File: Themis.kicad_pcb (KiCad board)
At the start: 2 copper layers, 100 x 50 mm, 585 parts, among them J1 SMA, J10 Conn_01x01, J11 Conn_01x01, J12 Conn_01x01, J13 Conn_01x01, J14 SMA, J15 SMA, J16 SMA, J17 SMA, J18 Conn_01x01, J2 SMA, J20 Conn_01x01, J3 SMA, J4 SMA, J5 Conn_01x05, J6 SMA, J7 SMA, J8 SMA, J9 SMA, T1 Tr 1/33, T2 Tr 33/1, U1 LMC6482

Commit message: new stitching, new gerber
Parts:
- removed the REF** at (101.5, 126.0)
- removed the REF** at (100.5, 126.0)
- removed the REF** at (99.5, 126.0)
- removed the REF** at (98.5, 126.0)
- removed the REF** at (97.5, 126.0)
- removed the REF** at (96.5, 126.0)
- removed the REF** at (95.5, 126.0)
- removed the REF** at (101.5, 125.0)
- removed the REF** at (100.5, 125.0)
- removed the REF** at (99.5, 125.0)
- removed the REF** at (98.5, 125.0)
- removed the REF** at (97.5, 125.0)
- removed the REF** at (96.5, 125.0)
- removed the REF** at (95.5, 125.0)
- removed the REF** at (101.5, 124.0)
- removed the REF** at (100.5, 124.0)
- removed the REF** at (99.5, 124.0)
- removed the REF** at (98.5, 124.0)
- removed the REF** at (97.5, 124.0)
- removed the REF** at (96.5, 124.0)
- removed the REF** at (95.5, 124.0)
- removed the REF** at (101.5, 123.0)
- removed the REF** at (100.5, 123.0)
- removed the REF** at (99.5, 123.0)
- removed the REF** at (98.5, 123.0)
- removed the REF** at (97.5, 123.0)
- removed the REF** at (96.5, 123.0)
- removed the REF** at (95.5, 123.0)
- removed the REF** at (101.5, 122.0)
- removed the REF** at (100.5, 122.0)
- removed the REF** at (99.5, 122.0)
- removed the REF** at (98.5, 122.0)
- removed the REF** at (97.5, 122.0)
- removed the REF** at (96.5, 122.0)
- removed the REF** at (95.5, 122.0)
- removed the REF** at (101.5, 121.0)
- removed the REF** at (100.5, 121.0)
- removed the REF** at (99.5, 121.0)
- removed the REF** at (98.5, 121.0)
- removed the REF** at (97.5, 121.0)
- removed the REF** at (96.5, 121.0)
- removed the REF** at (95.5, 121.0)
- removed the REF** at (101.5, 120.0)
- removed the REF** at (100.5, 120.0)
- removed the REF** at (99.5, 120.0)
- removed the REF** at (98.5, 120.0)
- removed the REF** at (97.5, 120.0)
- removed the REF** at (96.5, 120.0)
- removed the REF** at (95.5, 120.0)
- removed the REF** at (101.5, 119.0)
- removed the REF** at (100.5, 119.0)
- removed the REF** at (99.5, 119.0)
- removed the REF** at (98.5, 119.0)
- removed the REF** at (97.5, 119.0)
- removed the REF** at (96.5, 119.0)
- removed the REF** at (95.5, 119.0)
- removed the REF** at (101.5, 118.0)
- removed the REF** at (100.5, 118.0)
- removed the REF** at (99.5, 118.0)
- removed the REF** at (98.5, 118.0)
- removed the REF** at (97.5, 118.0)
- removed the REF** at (96.5, 118.0)
- removed the REF** at (95.5, 118.0)
- removed the REF** at (101.5, 117.0)
- removed the REF** at (100.5, 117.0)
- removed the REF** at (99.5, 117.0)
- removed the REF** at (98.5, 117.0)
- removed the REF** at (97.5, 117.0)
- removed the REF** at (96.5, 117.0)
- removed the REF** at (95.5, 117.0)
- removed the REF** at (101.5, 116.0)
- removed the REF** at (100.5, 116.0)
- removed the REF** at (99.5, 116.0)
- removed the REF** at (98.5, 116.0)
- removed the REF** at (97.5, 116.0)
- removed the REF** at (96.5, 116.0)
- removed the REF** at (95.5, 116.0)
- removed the REF** at (101.5, 115.0)
- removed the REF** at (100.5, 115.0)
- removed the REF** at (99.5, 115.0)
- removed the REF** at (98.5, 115.0)
- removed the REF** at (97.5, 115.0)
- removed the REF** at (96.5, 115.0)
- removed the REF** at (95.5, 115.0)
- removed the REF** at (101.5, 114.0)
- removed the REF** at (100.5, 114.0)
- removed the REF** at (99.5, 114.0)
- removed the REF** at (98.5, 114.0)
- removed the REF** at (97.5, 114.0)
- removed the REF** at (96.5, 114.0)
- removed the REF** at (95.5, 114.0)
- removed the REF** at (101.5, 113.0)
- removed the REF** at (100.5, 113.0)
- removed the REF** at (99.5, 113.0)
- removed the REF** at (98.5, 113.0)
- removed the REF** at (97.5, 113.0)
- removed the REF** at (96.5, 113.0)
- removed the REF** at (95.5, 113.0)
- removed the REF** at (101.5, 112.0)
- removed the REF** at (100.5, 112.0)
- removed the REF** at (99.5, 112.0)
- removed the REF** at (98.5, 112.0)
- removed the REF** at (97.5, 112.0)
- removed the REF** at (96.5, 112.0)
- removed the REF** at (95.5, 112.0)
- removed the REF** at (101.5, 111.0)
- removed the REF** at (100.5, 111.0)
- removed the REF** at (99.5, 111.0)
- removed the REF** at (98.5, 111.0)
- removed the REF** at (97.5, 111.0)
- removed the REF** at (96.5, 111.0)
- removed the REF** at (95.5, 111.0)
- removed the REF** at (185.0, 126.0)
- removed the REF** at (184.0, 126.0)
- removed the REF** at (183.0, 126.0)
- removed the REF** at (182.0, 126.0)
- removed the REF** at (181.0, 126.0)
- removed the REF** at (180.0, 126.0)
- removed the REF** at (179.0, 126.0)
- removed the REF** at (178.0, 126.0)
- removed the REF** at (185.0, 125.0)
- removed the REF** at (184.0, 125.0)
- removed the REF** at (183.0, 125.0)
- removed the REF** at (182.0, 125.0)
- removed the REF** at (181.0, 125.0)
- removed the REF** at (180.0, 125.0)
- removed the REF** at (179.0, 125.0)
- removed the REF** at (178.0, 125.0)
- removed the REF** at (185.0, 124.0)
- removed the REF** at (184.0, 124.0)
- removed the REF** at (183.0, 124.0)
- removed the REF** at (182.0, 124.0)
- removed the REF** at (181.0, 124.0)
- removed the REF** at (180.0, 124.0)
- removed the REF** at (179.0, 124.0)
- removed the REF** at (178.0, 124.0)
- removed the REF** at (185.0, 123.0)
- removed the REF** at (184.0, 123.0)
- removed the REF** at (183.0, 123.0)
- removed the REF** at (182.0, 123.0)
- removed the REF** at (181.0, 123.0)
- removed the REF** at (180.0, 123.0)
- removed the REF** at (179.0, 123.0)
- removed the REF** at (178.0, 123.0)
- removed the REF** at (185.0, 122.0)
- removed the REF** at (184.0, 122.0)
- removed the REF** at (183.0, 122.0)
- removed the REF** at (182.0, 122.0)
- removed the REF** at (181.0, 122.0)
- removed the REF** at (180.0, 122.0)
- removed the REF** at (179.0, 122.0)
- removed the REF** at (178.0, 122.0)
- removed the REF** at (185.0, 121.0)
- removed the REF** at (184.0, 121.0)
- removed the REF** at (183.0, 121.0)
- removed the REF** at (182.0, 121.0)
- removed the REF** at (181.0, 121.0)
- removed the REF** at (180.0, 121.0)
- removed the REF** at (179.0, 121.0)
- removed the REF** at (178.0, 121.0)
- removed the REF** at (185.0, 120.0)
- removed the REF** at (184.0, 120.0)
- removed the REF** at (183.0, 120.0)
- removed the REF** at (182.0, 120.0)
- removed the REF** at (181.0, 120.0)
- removed the REF** at (180.0, 120.0)
- removed the REF** at (179.0, 120.0)
- removed the REF** at (178.0, 120.0)
- removed the REF** at (185.0, 119.0)
- removed the REF** at (184.0, 119.0)
- removed the REF** at (183.0, 119.0)
- removed the REF** at (182.0, 119.0)
- removed the REF** at (181.0, 119.0)
- removed the REF** at (180.0, 119.0)
- removed the REF** at (179.0, 119.0)
- removed the REF** at (178.0, 119.0)
- removed the REF** at (185.0, 118.0)
- removed the REF** at (184.0, 118.0)
- removed the REF** at (183.0, 118.0)
- removed the REF** at (182.0, 118.0)
- removed the REF** at (181.0, 118.0)
- removed the REF** at (180.0, 118.0)
- removed the REF** at (179.0, 118.0)
- removed the REF** at (178.0, 118.0)
- removed the REF** at (185.0, 117.0)
- removed the REF** at (184.0, 117.0)
- removed the REF** at (183.0, 117.0)
- removed the REF** at (182.0, 117.0)
- removed the REF** at (181.0, 117.0)
- removed the REF** at (180.0, 117.0)
- removed the REF** at (179.0, 117.0)
- removed the REF** at (178.0, 117.0)
- removed the REF** at (185.0, 116.0)
- removed the REF** at (184.0, 116.0)
- removed the REF** at (183.0, 116.0)
- removed the REF** at (182.0, 116.0)
- removed the REF** at (181.0, 116.0)
- removed the REF** at (180.0, 116.0)
- removed the REF** at (179.0, 116.0)
- removed the REF** at (178.0, 116.0)
- removed the REF** at (185.0, 115.0)
- removed the REF** at (184.0, 115.0)
- removed the REF** at (183.0, 115.0)
- removed the REF** at (182.0, 115.0)
- removed the REF** at (181.0, 115.0)
- removed the REF** at (180.0, 115.0)
- removed the REF** at (179.0, 115.0)
- removed the REF** at (178.0, 115.0)
- removed the REF** at (185.0, 114.0)
- removed the REF** at (184.0, 114.0)
- removed the REF** at (183.0, 114.0)
- removed the REF** at (182.0, 114.0)
- removed the REF** at (181.0, 114.0)
- removed the REF** at (180.0, 114.0)
- removed the REF** at (179.0, 114.0)
- removed the REF** at (178.0, 114.0)
- removed the REF** at (185.0, 113.0)
- removed the REF** at (184.0, 113.0)
- removed the REF** at (183.0, 113.0)
- removed the REF** at (182.0, 113.0)
- removed the REF** at (181.0, 113.0)
- removed the REF** at (180.0, 113.0)
- removed the REF** at (179.0, 113.0)
- removed the REF** at (178.0, 113.0)
- removed the REF** at (185.0, 112.0)
- removed the REF** at (184.0, 112.0)
- removed the REF** at (183.0, 112.0)
- removed the REF** at (182.0, 112.0)
- removed the REF** at (181.0, 112.0)
- removed the REF** at (180.0, 112.0)
- removed the REF** at (179.0, 112.0)
- removed the REF** at (178.0, 112.0)
- removed the REF** at (185.0, 111.0)
- removed the REF** at (184.0, 111.0)
- removed the REF** at (183.0, 111.0)
- removed the REF** at (182.0, 111.0)
- removed the REF** at (181.0, 111.0)
- removed the REF** at (180.0, 111.0)
- removed the REF** at (179.0, 111.0)
- removed the REF** at (178.0, 111.0)
- added REF**: via, via:via, F.Cu at (186.0, 94.0)
- added REF**: via, via:via, F.Cu at (187.0, 98.0)
- added REF**: via, via:via, F.Cu at (120.0, 90.0)
- added REF**: via, via:via, F.Cu at (119.0, 90.0)
- added REF**: via, via:via, F.Cu at (118.0, 90.0)
- added REF**: via, via:via, F.Cu at (117.0, 90.0)
- added REF**: via, via:via, F.Cu at (116.0, 90.0)
- added REF**: via, via:via, F.Cu at (115.0, 90.0)
- added REF**: via, via:via, F.Cu at (114.0, 90.0)
- added REF**: via, via:via, F.Cu at (113.0, 90.0)
- added REF**: via, via:via, F.Cu at (112.0, 90.0)
- added REF**: via, via:via, F.Cu at (111.0, 90.0)
- added REF**: via, via:via, F.Cu at (186.0, 99.0)
- added REF**: via, via:via, F.Cu at (110.0, 90.0)
- added REF**: via, via:via, F.Cu at (109.0, 90.0)
- added REF**: via, via:via, F.Cu at (108.0, 90.0)
- added REF**: via, via:via, F.Cu at (107.0, 90.0)
- added REF**: via, via:via, F.Cu at (106.0, 90.0)
- added REF**: via, via:via, F.Cu at (105.0, 90.0)
- added REF**: via, via:via, F.Cu at (104.0, 90.0)
- added REF**: via, via:via, F.Cu at (103.0, 90.0)
- added REF**: via, via:via, F.Cu at (102.0, 90.0)
- added REF**: via, via:via, F.Cu at (101.0, 90.0)
- added REF**: via, via:via, F.Cu at (187.0, 99.0)
- added REF**: via, via:via, F.Cu at (100.0, 90.0)
- added REF**: via, via:via, F.Cu at (99.0, 90.0)
- added REF**: via, via:via, F.Cu at (127.0, 89.0)
- added REF**: via, via:via, F.Cu at (126.0, 89.0)
- added REF**: via, via:via, F.Cu at (125.0, 89.0)
- added REF**: via, via:via, F.Cu at (124.0, 89.0)
- added REF**: via, via:via, F.Cu at (123.0, 89.0)
- added REF**: via, via:via, F.Cu at (122.0, 89.0)
- added REF**: via, via:via, F.Cu at (121.0, 89.0)
- added REF**: via, via:via, F.Cu at (120.0, 89.0)
- added REF**: via, via:via, F.Cu at (186.0, 100.0)
- added REF**: via, via:via, F.Cu at (119.0, 89.0)
- added REF**: via, via:via, F.Cu at (118.0, 89.0)
- added REF**: via, via:via, F.Cu at (117.0, 89.0)
- added REF**: via, via:via, F.Cu at (116.0, 89.0)
- added REF**: via, via:via, F.Cu at (115.0, 89.0)
- added REF**: via, via:via, F.Cu at (114.0, 89.0)
- added REF**: via, via:via, F.Cu at (113.0, 89.0)
- added REF**: via, via:via, F.Cu at (112.0, 89.0)
- added REF**: via, via:via, F.Cu at (111.0, 89.0)
- added REF**: via, via:via, F.Cu at (110.0, 89.0)
- added REF**: via, via:via, F.Cu at (187.0, 100.0)
- added REF**: via, via:via, F.Cu at (109.0, 89.0)
- added REF**: via, via:via, F.Cu at (108.0, 89.0)
- added REF**: via, via:via, F.Cu at (107.0, 89.0)
- added REF**: via, via:via, F.Cu at (106.0, 89.0)
- added REF**: via, via:via, F.Cu at (105.0, 89.0)
- added REF**: via, via:via, F.Cu at (104.0, 89.0)
- added REF**: via, via:via, F.Cu at (103.0, 89.0)
- added REF**: via, via:via, F.Cu at (102.0, 89.0)
- added REF**: via, via:via, F.Cu at (101.0, 89.0)
- added REF**: via, via:via, F.Cu at (100.0, 89.0)
- added REF**: via, via:via, F.Cu at (188.0, 94.0)
- added REF**: via, via:via, F.Cu at (99.0, 89.0)
- added REF**: via, via:via, F.Cu at (127.0, 88.0)
- added REF**: via, via:via, F.Cu at (126.0, 88.0)
- added REF**: via, via:via, F.Cu at (125.0, 88.0)
- added REF**: via, via:via, F.Cu at (124.0, 88.0)
- added REF**: via, via:via, F.Cu at (123.0, 88.0)
- added REF**: via, via:via, F.Cu at (122.0, 88.0)
- added REF**: via, via:via, F.Cu at (121.0, 88.0)
- added REF**: via, via:via, F.Cu at (120.0, 88.0)
- added REF**: via, via:via, F.Cu at (119.0, 88.0)
- added REF**: via, via:via, F.Cu at (188.0, 95.0)
- added REF**: via, via:via, F.Cu at (118.0, 88.0)
- added REF**: via, via:via, F.Cu at (117.0, 88.0)
- added REF**: via, via:via, F.Cu at (116.0, 88.0)
- added REF**: via, via:via, F.Cu at (115.0, 88.0)
- added REF**: via, via:via, F.Cu at (114.0, 88.0)
- added REF**: via, via:via, F.Cu at (113.0, 88.0)
- added REF**: via, via:via, F.Cu at (112.0, 88.0)
- added REF**: via, via:via, F.Cu at (111.0, 88.0)
- added REF**: via, via:via, F.Cu at (110.0, 88.0)
- added REF**: via, via:via, F.Cu at (109.0, 88.0)
- added REF**: via, via:via, F.Cu at (188.0, 96.0)
- added REF**: via, via:via, F.Cu at (108.0, 88.0)
- added REF**: via, via:via, F.Cu at (107.0, 88.0)
- added REF**: via, via:via, F.Cu at (106.0, 88.0)
- added REF**: via, via:via, F.Cu at (105.0, 88.0)
- added REF**: via, via:via, F.Cu at (104.0, 88.0)
- added REF**: via, via:via, F.Cu at (103.0, 88.0)
- added REF**: via, via:via, F.Cu at (102.0, 88.0)
- added REF**: via, via:via, F.Cu at (101.0, 88.0)
- added REF**: via, via:via, F.Cu at (100.0, 88.0)
- added REF**: via, via:via, F.Cu at (99.0, 88.0)
- added REF**: via, via:via, F.Cu at (188.0, 97.0)
- added REF**: via, via:via, F.Cu at (127.0, 87.0)
- added REF**: via, via:via, F.Cu at (126.0, 87.0)
- added REF**: via, via:via, F.Cu at (125.0, 87.0)
- added REF**: via, via:via, F.Cu at (124.0, 87.0)
- added REF**: via, via:via, F.Cu at (123.0, 87.0)
- added REF**: via, via:via, F.Cu at (122.0, 87.0)
- added REF**: via, via:via, F.Cu at (121.0, 87.0)
- added REF**: via, via:via, F.Cu at (120.0, 87.0)
- added REF**: via, via:via, F.Cu at (119.0, 87.0)
- added REF**: via, via:via, F.Cu at (118.0, 87.0)
- added REF**: via, via:via, F.Cu at (188.0, 98.0)
- added REF**: via, via:via, F.Cu at (117.0, 87.0)
- added REF**: via, via:via, F.Cu at (116.0, 87.0)
- added REF**: via, via:via, F.Cu at (115.0, 87.0)
- added REF**: via, via:via, F.Cu at (114.0, 87.0)
- added REF**: via, via:via, F.Cu at (113.0, 87.0)
- added REF**: via, via:via, F.Cu at (112.0, 87.0)
- added REF**: via, via:via, F.Cu at (111.0, 87.0)
- added REF**: via, via:via, F.Cu at (110.0, 87.0)
- added REF**: via, via:via, F.Cu at (109.0, 87.0)
- added REF**: via, via:via, F.Cu at (108.0, 87.0)
- added REF**: via, via:via, F.Cu at (187.0, 94.0)
- added REF**: via, via:via, F.Cu at (188.0, 99.0)
- added REF**: via, via:via, F.Cu at (107.0, 87.0)
- added REF**: via, via:via, F.Cu at (106.0, 87.0)
- added REF**: via, via:via, F.Cu at (105.0, 87.0)
- added REF**: via, via:via, F.Cu at (104.0, 87.0)
- added REF**: via, via:via, F.Cu at (103.0, 87.0)
- added REF**: via, via:via, F.Cu at (102.0, 87.0)
- added REF**: via, via:via, F.Cu at (101.0, 87.0)
- added REF**: via, via:via, F.Cu at (100.0, 87.0)
- added REF**: via, via:via, F.Cu at (99.0, 87.0)
- added REF**: via, via:via, F.Cu at (91.0, 101.0)
- added REF**: via, via:via, F.Cu at (188.0, 100.0)
- added REF**: via, via:via, F.Cu at (91.0, 100.0)
- added REF**: via, via:via, F.Cu at (91.0, 99.0)
- added REF**: via, via:via, F.Cu at (91.0, 98.0)
- added REF**: via, via:via, F.Cu at (91.0, 97.0)
- added REF**: via, via:via, F.Cu at (91.0, 96.0)
- added REF**: via, via:via, F.Cu at (91.0, 95.0)
- added REF**: via, via:via, F.Cu at (91.0, 94.0)
- added REF**: via, via:via, F.Cu at (91.0, 93.0)
- added REF**: via, via:via, F.Cu at (91.0, 92.0)
- added REF**: via, via:via, F.Cu at (91.0, 91.0)
- added REF**: via, via:via, F.Cu at (93.0, 94.0)
- added REF**: via, via:via, F.Cu at (91.0, 90.0)
- added REF**: via, via:via, F.Cu at (91.0, 89.0)
- added REF**: via, via:via, F.Cu at (91.0, 88.0)
- added REF**: via, via:via, F.Cu at (91.0, 87.0)
- added REF**: via, via:via, F.Cu at (94.0, 94.0)
- added REF**: via, via:via, F.Cu at (95.0, 94.0)
- added REF**: via, via:via, F.Cu at (93.0, 95.0)
- added REF**: via, via:via, F.Cu at (94.0, 95.0)
- added REF**: via, via:via, F.Cu at (95.0, 95.0)
- added REF**: via, via:via, F.Cu at (93.0, 96.0)
- added REF**: via, via:via, F.Cu at (94.0, 96.0)
- added REF**: via, via:via, F.Cu at (186.0, 95.0)
- added REF**: via, via:via, F.Cu at (95.0, 96.0)
- added REF**: via, via:via, F.Cu at (93.0, 97.0)
- added REF**: via, via:via, F.Cu at (94.0, 97.0)
- added REF**: via, via:via, F.Cu at (95.0, 97.0)
- added REF**: via, via:via, F.Cu at (93.0, 98.0)
- added REF**: via, via:via, F.Cu at (94.0, 98.0)
- added REF**: via, via:via, F.Cu at (95.0, 98.0)
- added REF**: via, via:via, F.Cu at (93.0, 99.0)
- added REF**: via, via:via, F.Cu at (94.0, 99.0)
- added REF**: via, via:via, F.Cu at (95.0, 99.0)
- added REF**: via, via:via, F.Cu at (187.0, 95.0)
- added REF**: via, via:via, F.Cu at (92.0, 94.0)
- added REF**: via, via:via, F.Cu at (92.0, 95.0)
- added REF**: via, via:via, F.Cu at (92.0, 96.0)
- added REF**: via, via:via, F.Cu at (92.0, 97.0)
- added REF**: via, via:via, F.Cu at (92.0, 98.0)
- added REF**: via, via:via, F.Cu at (92.0, 99.0)
- added REF**: via, via:via, F.Cu at (188.0, 128.0)
- added REF**: via, via:via, F.Cu at (188.0, 127.0)
- added REF**: via, via:via, F.Cu at (188.0, 126.0)
- added REF**: via, via:via, F.Cu at (188.0, 125.0)
- added REF**: via, via:via, F.Cu at (186.0, 96.0)
- added REF**: via, via:via, F.Cu at (188.0, 124.0)
- added REF**: via, via:via, F.Cu at (188.0, 123.0)
- added REF**: via, via:via, F.Cu at (188.0, 122.0)
- added REF**: via, via:via, F.Cu at (188.0, 121.0)
- added REF**: via, via:via, F.Cu at (188.0, 120.0)
- added REF**: via, via:via, F.Cu at (188.0, 119.0)
- added REF**: via, via:via, F.Cu at (188.0, 118.0)
- added REF**: via, via:via, F.Cu at (188.0, 117.0)
- added REF**: via, via:via, F.Cu at (188.0, 116.0)
- added REF**: via, via:via, F.Cu at (188.0, 115.0)
- added REF**: via, via:via, F.Cu at (187.0, 96.0)
- added REF**: via, via:via, F.Cu at (188.0, 114.0)
- added REF**: via, via:via, F.Cu at (188.0, 113.0)
- added REF**: via, via:via, F.Cu at (188.0, 112.0)
- added REF**: via, via:via, F.Cu at (188.0, 111.0)
- added REF**: via, via:via, F.Cu at (127.0, 91.0)
- added REF**: via, via:via, F.Cu at (126.0, 91.0)
- added REF**: via, via:via, F.Cu at (125.0, 91.0)
- added REF**: via, via:via, F.Cu at (124.0, 91.0)
- added REF**: via, via:via, F.Cu at (123.0, 91.0)
- added REF**: via, via:via, F.Cu at (122.0, 91.0)
- added REF**: via, via:via, F.Cu at (186.0, 97.0)
- added REF**: via, via:via, F.Cu at (121.0, 91.0)
- added REF**: via, via:via, F.Cu at (120.0, 91.0)
- added REF**: via, via:via, F.Cu at (119.0, 91.0)
- added REF**: via, via:via, F.Cu at (118.0, 91.0)
- added REF**: via, via:via, F.Cu at (117.0, 91.0)
- added REF**: via, via:via, F.Cu at (116.0, 91.0)
- added REF**: via, via:via, F.Cu at (115.0, 91.0)
- added REF**: via, via:via, F.Cu at (114.0, 91.0)
- added REF**: via, via:via, F.Cu at (113.0, 91.0)
- added REF**: via, via:via, F.Cu at (112.0, 91.0)
- added REF**: via, via:via, F.Cu at (187.0, 97.0)
- added REF**: via, via:via, F.Cu at (111.0, 91.0)
- added REF**: via, via:via, F.Cu at (110.0, 91.0)
- added REF**: via, via:via, F.Cu at (109.0, 91.0)
- added REF**: via, via:via, F.Cu at (108.0, 91.0)
- added REF**: via, via:via, F.Cu at (107.0, 91.0)
- added REF**: via, via:via, F.Cu at (106.0, 91.0)
- added REF**: via, via:via, F.Cu at (105.0, 91.0)
- added REF**: via, via:via, F.Cu at (104.0, 91.0)
- added REF**: via, via:via, F.Cu at (103.0, 91.0)
- added REF**: via, via:via, F.Cu at (102.0, 91.0)
- added REF**: via, via:via, F.Cu at (186.0, 98.0)
- added REF**: via, via:via, F.Cu at (101.0, 91.0)
- added REF**: via, via:via, F.Cu at (100.0, 91.0)
- added REF**: via, via:via, F.Cu at (99.0, 91.0)
- added REF**: via, via:via, F.Cu at (127.0, 90.0)
- added REF**: via, via:via, F.Cu at (126.0, 90.0)
- added REF**: via, via:via, F.Cu at (125.0, 90.0)
- added REF**: via, via:via, F.Cu at (124.0, 90.0)
- added REF**: via, via:via, F.Cu at (123.0, 90.0)
- added REF**: via, via:via, F.Cu at (122.0, 90.0)
- added REF**: via, via:via, F.Cu at (121.0, 90.0)
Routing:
- net GND: vias 361 -> 369

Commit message: new gerber added
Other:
- board text added: "RX1_Line"
- board text removed: "To RX1_Line"
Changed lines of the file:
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@@
     (links 644)
     (no_connects 0)
-    (area 89.924999 84.924999 190.075001 135.075001)
+    (area 80.724999 82.899999 225.428571 177.05)
     (thickness 1.6)
     (drawings 14)
@@
   )
   (setup
-    (last_trace_width 0.25)
+    (last_trace_width 2)
     (user_trace_width 0.6)
     (user_trace_width 1)
@@
     (effects (font (size 1.5 1.5) (thickness 0.3)))
   )
-  (gr_text "To\n RX1_Line" (at 121.5 112) (layer F.SilkS)
+  (gr_text " RX1_Line" (at 122.5 114) (layer F.SilkS)
     (effects (font (size 1.5 1.5) (thickness 0.3)))
   )
@@
   (segment (start 176.985 95) (end 176.985 101.985) (width 3) (layer F.Cu) (net 17))
   (segment (start 176.985 101.985) (end 180 105) (width 3) (layer F.Cu) (net 17))
-  (segment (start 185 105) (end 180 105) (width 1.6) (layer F.Cu) (net 17))
+  (segment (start 185 105) (end 180 105) (width 2) (layer F.Cu) (net 17))
   (segment (start 180 105) (end 176.985 101.985) (width 1.6) (layer F.Cu) (net 17))
   (segment (start 188 105) (end 185 105) (width 1.6) (layer F.Cu) (net 17))

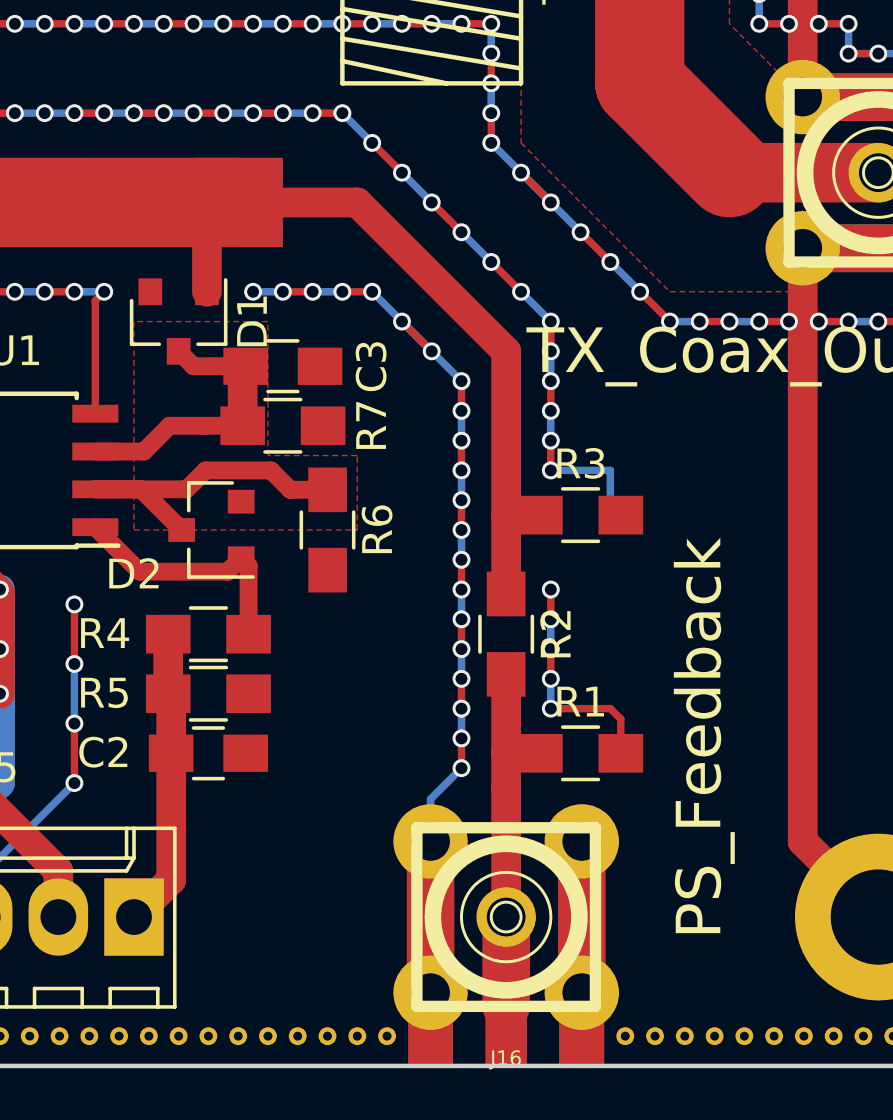
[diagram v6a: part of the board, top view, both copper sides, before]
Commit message: enlarged PS_Feedback trace
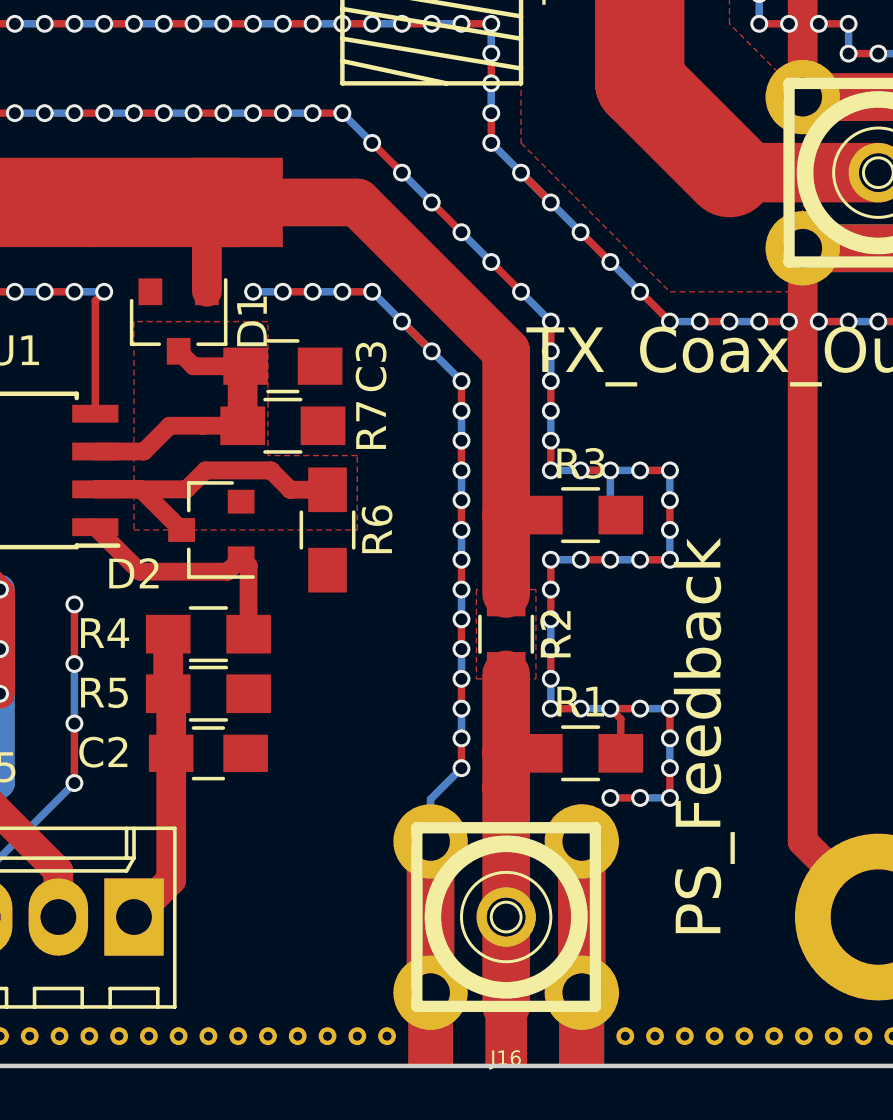
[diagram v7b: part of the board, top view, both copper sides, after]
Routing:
- net GND: track 761.5 -> 779.5 mm, vias 369 -> 389
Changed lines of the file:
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@@
     (thickness 1.6)
     (drawings 14)
-    (tracks 967)
+    (tracks 1007)
     (zones 0)
     (modules 568)
@@
   )
   (setup
-    (last_trace_width 2)
+    (last_trace_width 0.25)
     (user_trace_width 0.6)
     (user_trace_width 1)
@@
   (gr_line (start 190 85) (end 190 135) (angle 90) (layer Edge.Cuts) (width 0.15))
   (gr_line (start 90 85) (end 190 85) (angle 90) (layer Edge.Cuts) (width 0.15))
+  (segment (start 174 119) (end 174 118) (width 0.25) (layer F.Cu) (net 1))
+  (via (at 174 123) (size 0.6) (drill 0.4) (layers F.Cu B.Cu) (net 1))
+  (segment (start 174 123) (end 174 122) (width 0.25) (layer B.Cu) (net 1))
+  (via (at 174 122) (size 0.6) (drill 0.4) (layers F.Cu B.Cu) (net 1))
+  (segment (start 174 122) (end 174 121) (width 0.25) (layer F.Cu) (net 1))
+  (via (at 174 121) (size 0.6) (drill 0.4) (layers F.Cu B.Cu) (net 1))
+  (segment (start 174 121) (end 174 120) (width 0.25) (layer B.Cu) (net 1))
+  (via (at 174 120) (size 0.6) (drill 0.4) (layers F.Cu B.Cu) (net 1))
+  (segment (start 174 120) (end 174 119) (width 0.25) (layer F.Cu) (net 1))
+  (via (at 174 119) (size 0.6) (drill 0.4) (layers F.Cu B.Cu) (net 1))
+  (via (at 175 123) (size 0.6) (drill 0.4) (layers F.Cu B.Cu) (net 1))
+  (segment (start 176 123) (end 175 123) (width 0.25) (layer B.Cu) (net 1))
+  (via (at 176 123) (size 0.6) (drill 0.4) (layers F.Cu B.Cu) (net 1))
+  (segment (start 174 123) (end 175 123) (width 0.25) (layer F.Cu) (net 1))
+  (segment (start 177 115) (end 176 115) (width 0.25) (layer B.Cu) (net 1))
+  (via (at 177 115) (size 0.6) (drill 0.4) (layers F.Cu B.Cu) (net 1))
+  (segment (start 178 115) (end 177 115) (width 0.25) (layer F.Cu) (net 1))
+  (via (at 178 115) (size 0.6) (drill 0.4) (layers F.Cu B.Cu) (net 1))
+  (segment (start 178 116) (end 178 115) (width 0.25) (layer B.Cu) (net 1))
+  (via (at 178 116) (size 0.6) (drill 0.4) (layers F.Cu B.Cu) (net 1))
+  (segment (start 178 117) (end 178 116) (width 0.25) (layer F.Cu) (net 1))
+  (via (at 178 117) (size 0.6) (drill 0.4) (layers F.Cu B.Cu) (net 1))
+  (segment (start 178 118) (end 178 117) (width 0.25) (layer B.Cu) (net 1))
+  (via (at 178 118) (size 0.6) (drill 0.4) (layers F.Cu B.Cu) (net 1))
+  (segment (start 177 118) (end 178 118) (width 0.25) (layer F.Cu) (net 1))
+  (via (at 177 118) (size 0.6) (drill 0.4) (layers F.Cu B.Cu) (net 1))
+  (segment (start 176 118) (end 177 118) (width 0.25) (layer B.Cu) (net 1))
+  (via (at 176 118) (size 0.6) (drill 0.4) (layers F.Cu B.Cu) (net 1))
+  (segment (start 175 118) (end 176 118) (width 0.25) (layer F.Cu) (net 1))
+  (via (at 175 118) (size 0.6) (drill 0.4) (layers F.Cu B.Cu) (net 1))
+  (segment (start 174 118) (end 175 118) (width 0.25) (layer B.Cu) (net 1))
+  (via (at 174 118) (size 0.6) (drill 0.4) (layers F.Cu B.Cu) (net 1))
+  (via (at 176 115) (size 0.6) (drill 0.4) (layers F.Cu B.Cu) (net 1))
+  (via (at 175 115) (size 0.6) (drill 0.4) (layers F.Cu B.Cu) (net 1))
+  (segment (start 176 115) (end 175 115) (width 0.25) (layer F.Cu) (net 1))
+  (segment (start 176 123) (end 177 123) (width 0.25) (layer F.Cu) (net 1))
+  (via (at 176 126) (size 0.6) (drill 0.4) (layers F.Cu B.Cu) (net 1))
+  (segment (start 177 126) (end 176 126) (width 0.25) (layer F.Cu) (net 1))
+  (via (at 177 126) (size 0.6) (drill 0.4) (layers F.Cu B.Cu) (net 1))
+  (segment (start 178 126) (end 177 126) (width 0.25) (layer B.Cu) (net 1))
+  (via (at 178 126) (size 0.6) (drill 0.4) (layers F.Cu B.Cu) (net 1))
+  (segment (start 178 125) (end 178 126) (width 0.25) (layer F.Cu) (net 1))
+  (via (at 178 125) (size 0.6) (drill 0.4) (layers F.Cu B.Cu) (net 1))
+  (segment (start 178 124) (end 178 125) (width 0.25) (layer B.Cu) (net 1))
+  (via (at 178 124) (size 0.6) (drill 0.4) (layers F.Cu B.Cu) (net 1))
+  (segment (start 178 123) (end 178 124) (width 0.25) (layer F.Cu) (net 1))
+  (via (at 178 123) (size 0.6) (drill 0.4) (layers F.Cu B.Cu) (net 1))
+  (segment (start 177 123) (end 178 123) (width 0.25) (layer B.Cu) (net 1))
+  (via (at 177 123) (size 0.6) (drill 0.4) (layers F.Cu B.Cu) (net 1))
   (segment (start 131 134) (end 132 134) (width 0.25) (layer F.Cu) (net 1))
   (segment (start 130 134) (end 131 134) (width 0.25) (layer F.Cu) (net 1))
@@
   (segment (start 174 115) (end 174 114) (width 0.25) (layer F.Cu) (net 1))
   (via (at 174 115) (size 0.6) (drill 0.4) (layers F.Cu B.Cu) (net 1))
-  (segment (start 176 115) (end 174 115) (width 0.25) (layer B.Cu) (net 1))
+  (segment (start 176 115) (end 175 115) (width 0.25) (layer B.Cu) (net 1))
+  (segment (start 175 115) (end 174 115) (width 0.25) (layer B.Cu) (net 1))
   (segment (start 176.35 124.5) (end 176.35 123.35) (width 0.25) (layer F.Cu) (net 1))
-  (via (at 174 119) (size 0.6) (drill 0.4) (layers F.Cu B.Cu) (net 1))
-  (segment (start 174 120) (end 174 119) (width 0.25) (layer F.Cu) (net 1))
-  (via (at 174 120) (size 0.6) (drill 0.4) (layers F.Cu B.Cu) (net 1))
-  (segment (start 174 121) (end 174 120) (width 0.25) (layer B.Cu) (net 1))
-  (via (at 174 121) (size 0.6) (drill 0.4) (layers F.Cu B.Cu) (net 1))
-  (segment (start 174 122) (end 174 121) (width 0.25) (layer F.Cu) (net 1))
-  (via (at 174 122) (size 0.6) (drill 0.4) (layers F.Cu B.Cu) (net 1))
-  (segment (start 174 123) (end 174 122) (width 0.25) (layer B.Cu) (net 1))
-  (via (at 174 123) (size 0.6) (drill 0.4) (layers F.Cu B.Cu) (net 1))
-  (segment (start 176 123) (end 174 123) (width 0.25) (layer F.Cu) (net 1))
   (segment (start 176.35 123.35) (end 176 123) (width 0.25) (layer F.Cu) (net 1))
   (segment (start 157 103) (end 158 103) (width 0.25) (layer B.Cu) (net 1))
@@
   (segment (start 144.5 113.5) (end 144.5 115.75) (width 1) (layer F.Cu) (net 5))
   (segment (start 151.75 124.5) (end 153.5 124.5) (width 1) (layer F.Cu) (net 6))
-  (segment (start 157.46 128.46) (end 157.46 130) (width 1) (layer F.Cu) (net 6))
   (segment (start 153.5 124.5) (end 157.46 128.46) (width 1) (layer F.Cu) (net 6))
+  (segment (start 157.46 128.46) (end 157.46 130) (width 1) (layer F.Cu) (net 6))
   (segment (start 151.85 120.5) (end 151.85 122.5) (width 1) (layer F.Cu) (net 6))
   (segment (start 151.85 122.5) (end 151.75 122.6) (width 1) (layer F.Cu) (net 6))
@@
   (segment (start 158.5 106) (end 154 106) (width 3) (layer F.Cu) (net 7))
   (segment (start 173.65 116.5) (end 172.5 116.5) (width 1) (layer F.Cu) (net 7))
-  (segment (start 172.5 119.15) (end 172.5 116.5) (width 1) (layer F.Cu) (net 7))
-  (segment (start 172.5 116.5) (end 172.5 111) (width 1) (layer F.Cu) (net 7))
-  (segment (start 167.5 106) (end 163.5 106) (width 1) (layer F.Cu) (net 7))
-  (segment (start 172.5 111) (end 167.5 106) (width 1) (layer F.Cu) (net 7))
+  (segment (start 172.5 119.15) (end 172.5 116.5) (width 1.6) (layer F.Cu) (net 7))
+  (segment (start 172.5 116.5) (end 172.5 111) (width 1.6) (layer F.Cu) (net 7))
+  (segment (start 172.5 111) (end 167.5 106) (width 1.6) (layer F.Cu) (net 7))
+  (segment (start 167.5 106) (end 163.5 106) (width 1.6) (layer F.Cu) (net 7))
   (segment (start 163.5 106) (end 158.5 106) (width 3) (layer F.Cu) (net 7))
   (segment (start 154 106) (end 149.85 106) (width 3) (layer F.Cu) (net 7))
@@
   (segment (start 137 133) (end 137 130) (width 1.6) (layer F.Cu) (net 18))
   (segment (start 173.65 124.5) (end 172.5 124.5) (width 1) (layer F.Cu) (net 19))
-  (segment (start 172.5 121.85) (end 172.5 124.5) (width 1) (layer F.Cu) (net 19))
-  (segment (start 172.5 124.5) (end 172.5 125.65) (width 1) (layer F.Cu) (net 19))
-  (segment (start 172.5 130) (end 172.5 125.65) (width 1) (layer F.Cu) (net 19))
+  (segment (start 172.5 121.85) (end 172.5 124.5) (width 1.6) (layer F.Cu) (net 19))
+  (segment (start 172.5 124.5) (end 172.5 125.65) (width 1.6) (layer F.Cu) (net 19))
+  (segment (start 172.5 130) (end 172.5 125.65) (width 1.6) (layer F.Cu) (net 19))
   (segment (start 172.5 133) (end 172.5 130) (width 1.6) (layer F.Cu) (net 19))
   (segment (start 114.5 126.25) (end 114.5 123.04) (width 1) (layer F.Cu) (net 20))
@@
       )
     )
+    (polygon
+      (pts        (xy 171.5 119) (xy 171.5 122) (xy 173.5 122) (xy 173.5 119)
+      )
+    )

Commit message: minor silk error fixed
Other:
- board text added: "Medium power Dual directionnal reflectometer"
- board text added: "Themis Θέμις"
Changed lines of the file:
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@@
     (links 644)
     (no_connects 0)
-    (area 80.724999 82.899999 225.428571 177.05)
+    (area 89.924999 84.924999 190.075001 135.075001)
     (thickness 1.6)
-    (drawings 14)
+    (drawings 17)
     (tracks 1007)
     (zones 0)
@@
       (net 1 GND) (zone_connect 2))
   )
+  (gr_text "Themis \nΘέμις\n" (at 118 100) (layer B.SilkS)
+    (effects (font (size 1.5 1.5) (thickness 0.3)) (justify mirror))
+  )
+  (gr_text "\nMedium power \nDual directionnal reflectometer" (at 161 93) (layer B.SilkS)
+    (effects (font (size 1.5 1.5) (thickness 0.3)) (justify mirror))
+  )
+  (gr_text "Themis \nΘέμις\n" (at 102 117) (layer F.SilkS)
+    (effects (font (size 1.5 1.5) (thickness 0.3)))
+  )
   (gr_line (start 156 111) (end 117 111) (angle 90) (layer Eco2.User) (width 0.2))
   (gr_line (start 156 110) (end 156 111) (angle 90) (layer Eco2.User) (width 0.2))
@@
     )
     (polygon
-      (pts        (xy 92 87) (xy 92 101) (xy 103 101) (xy 108 96) (xy 124 96)
-        (xy 129 91) (xy 155 91) (xy 155 87)
+      (pts        (xy 92 87) (xy 92 101) (xy 103 101) (xy 108 96) (xy 113 96)
+        (xy 113 94.6) (xy 117 94.6) (xy 117 96) (xy 124 96) (xy 129 91)
+        (xy 155 91) (xy 155 87)
       )
     )
